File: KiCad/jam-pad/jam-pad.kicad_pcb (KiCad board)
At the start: 2 copper layers, 131.4 x 57.1 mm, 82 parts, among them J1 USB_C, J2 PH_01x03_2.54mm, SW1 MX_Hotswap_LED_RGB, SW13 SW_Push, SW14 RotaryEncoder_Switch, SW15 SW_Push, SW2 MX_Hotswap_LED_RGB, SW3 MX_Hotswap_LED_RGB, SW4 MX_Hotswap_LED_RGB, SW5 MX_Hotswap_LED_RGB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

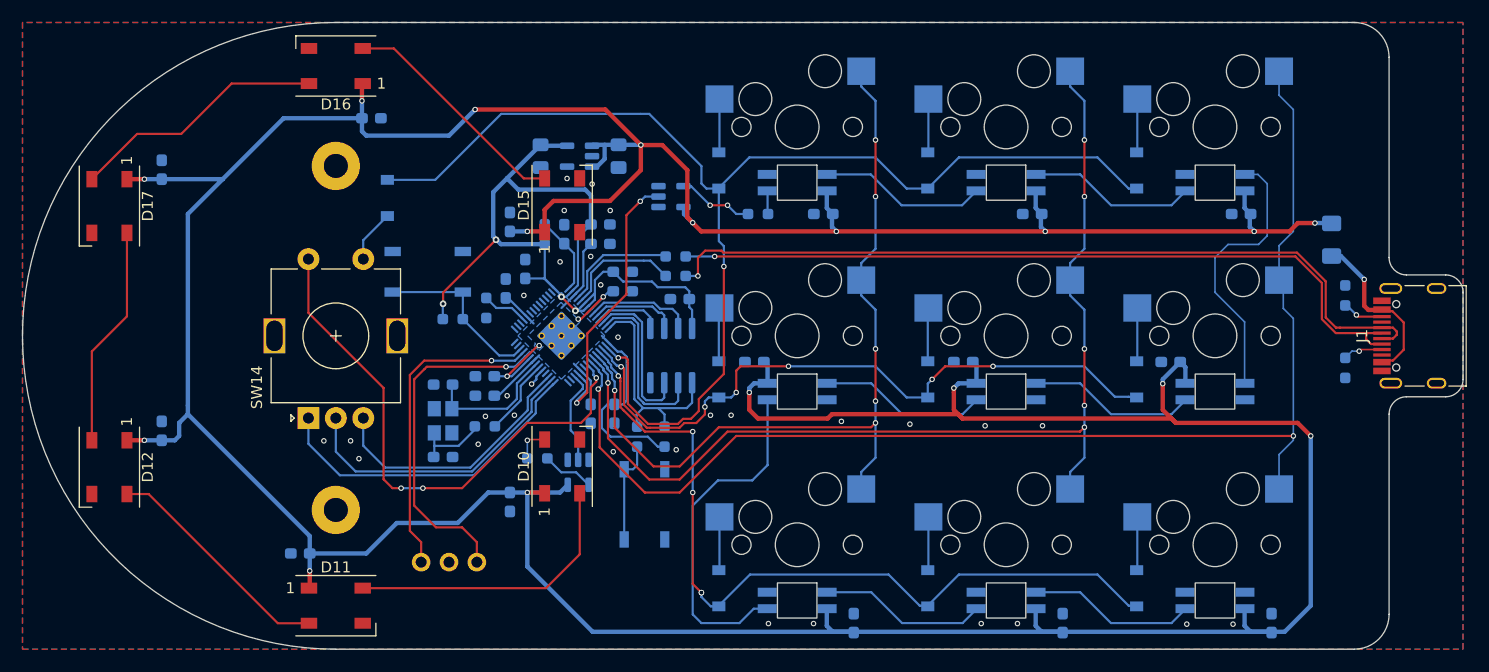
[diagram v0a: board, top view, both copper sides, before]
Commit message: fix up usb_boot; bare minimum gnd vias; fix silkscreen overlap
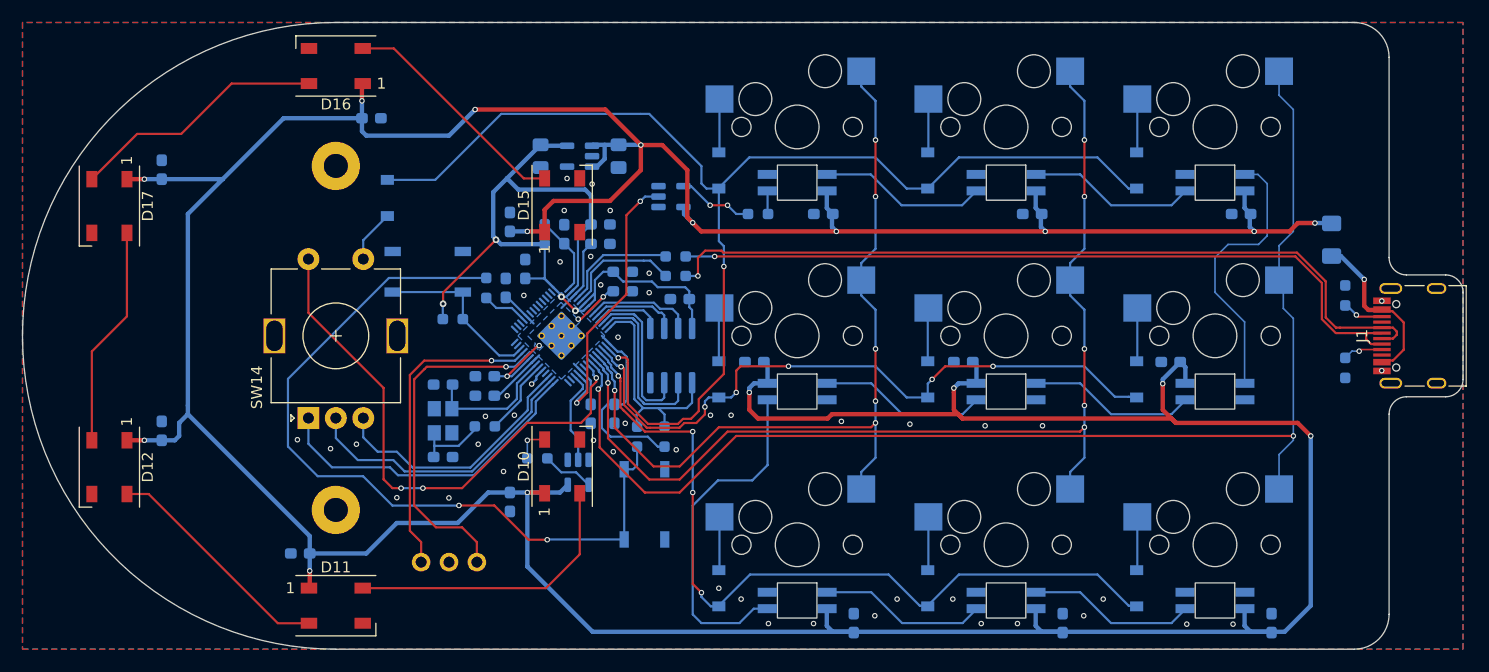
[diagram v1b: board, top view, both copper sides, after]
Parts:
- moved R9 1.83 mm to (74.0, 49.6), turned to 90 degrees
- moved C7 0.05 mm to (75.8, 49.6)
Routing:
- net /~{USB_BOOT}: track 9.42 -> 71.8 mm, vias 0 -> 2
- net /ENC_C: track 27.4 -> 26.7 mm
- net Row2: vias 5 -> 4
- net GND: vias 31 -> 47

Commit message: fab, clover logo, some other stuff? idr sorry
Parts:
- added Ref**: Val**, jam-pad:cloverlogo, B.Cu at (44.1, 54.0)
- moved D12 0.07 mm to (39.7, 65.9)
- moved D17 0.07 mm to (39.7, 42.1)
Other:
- board text added: "Brandon Gong and Ray Sun April 2023"
- board text added: "JAM PAD! v1.0"
- board text added: "JLCJLCJLCJLC"

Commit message: outdated case, updated pec11
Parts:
- SW14: footprint Keebio-Parts:RotaryEncoder_Alps_EC11E-Switch_Vertical_H20mm -> jam-pad:PEC11
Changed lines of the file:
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@@
     (pad "1" thru_hole circle (at 0 0) (size 4.4 4.4) (drill 2.2) (layers "*.Cu" "*.Mask"))
   )
-  (footprint "Keebio-Parts:RotaryEncoder_Alps_EC11E-Switch_Vertical_H20mm" (layer "F.Cu")
+  (footprint "jam-pad:PEC11" (layer "F.Cu")
     (at 60.325 53.975 90)
-    (descr "Alps rotary encoder, EC12E... with switch, vertical shaft, http://www.alps.com/prod/info/E/HTML/Encoder/Incremental/EC11/EC11E15204A3.html")
     (tags "rotary encoder")
     (property "JLCPCB_IGNORE" "Y")
@@
     (pad "S2" thru_hole circle (at 7 -2.5 90) (size 2 2) (drill 1) (layers "*.Cu" "*.Mask")
       (net 42 "Col3") (pinfunction "S2") (pintype "passive"))
-    (model "${KICAD6_3DMODEL_DIR}/Rotary_Encoder.3dshapes/RotaryEncoder_Alps_EC11E-Switch_Vertical_H20mm.wrl"
-      (offset (xyz 0 0 0))
+    (model "${KIPRJMOD}/3D_models/PEC11H-4215F-S0024.stp"
+      (offset (xyz -7.5 2.5 0))
       (scale (xyz 1 1 1))
-      (rotate (xyz 0 0 0))
+      (rotate (xyz 0 0 90))
     )
   )
